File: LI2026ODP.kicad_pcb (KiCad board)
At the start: 4 copper layers, 18.8 x 39.9 mm, 33 parts, among them J1 CON28-B700X1400_DIP, J2 Conn_01x05_Male, U1 MUA08A_TEX, U2 LQFP_0B1KET6_STM, U3 21-0066J_28_MXM

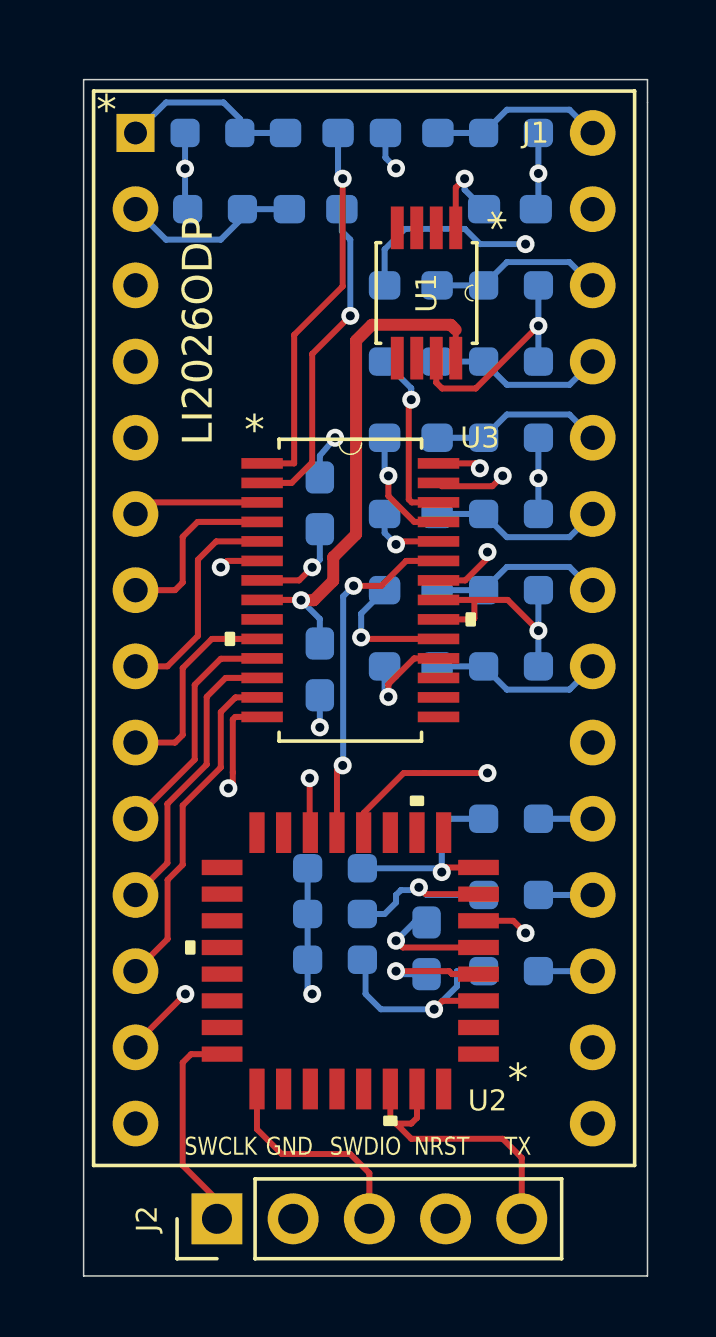
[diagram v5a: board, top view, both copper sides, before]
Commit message: Clean up the wire in the power layer.
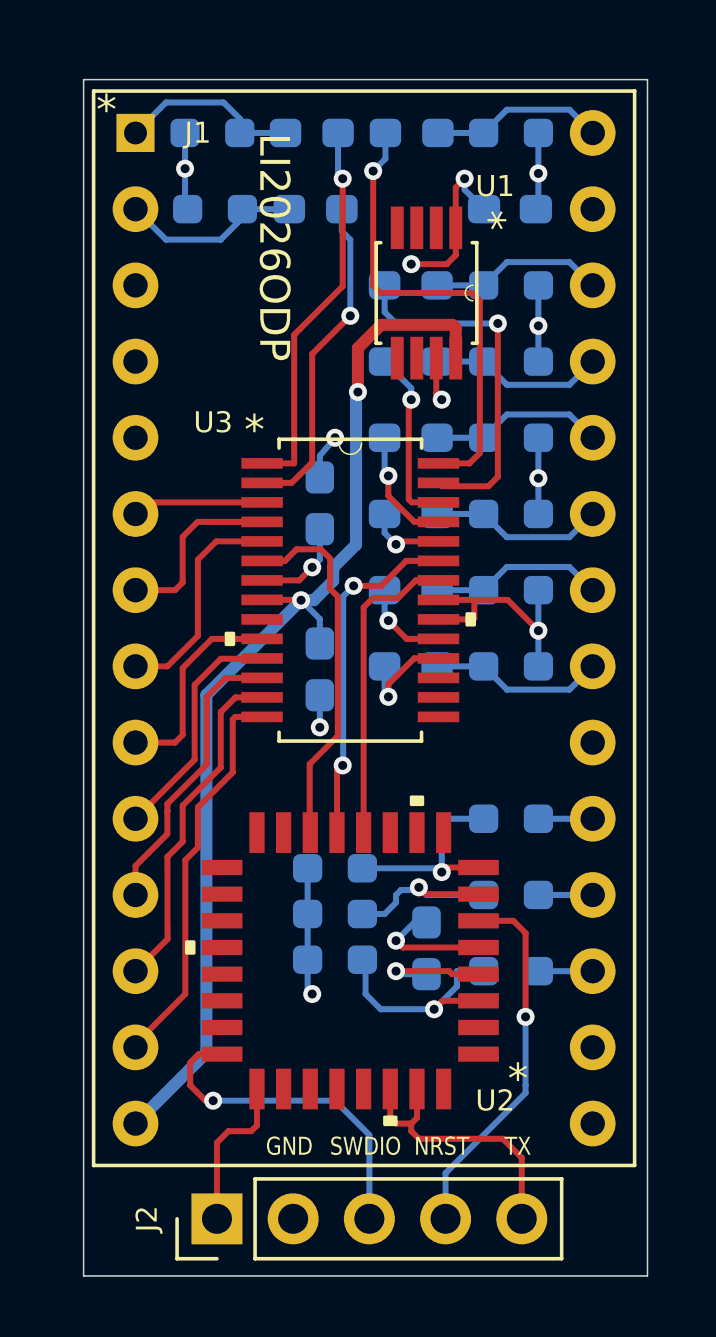
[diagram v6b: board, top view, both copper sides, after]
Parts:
- J1: value CON28-B700X1400_DIP -> 9-1437539-2
- U1: value MUA08A_TEX -> LM2936MM-3.3
- U2: value LQFP_0B1KET6_STM -> STM32G0B1KET6
- U3: value 21-0066J_28_MXM -> max6921aui
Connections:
- U2 pad 24: /SWCLK -> /SWDIO
- U2 pad 25: /SWDIO -> /SWCLK
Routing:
- net /D3: track 16.8 -> 12.1 mm, vias 2 -> 1
- net /SCK: track 14.9 -> 10.5 mm, vias 2 -> 0
- net /SWDIO: track 7.22 -> 11.4 mm, vias 0 -> 1
- net GND: track 34.5 -> 30.8 mm, vias 9 -> 10
- net +3V3: track 10.3 -> 12.8 mm, vias 3 -> 4
- net /D2: track 13.9 -> 15.6 mm, vias 2 -> 1
- net /D7: track 4.50 -> 2.99 mm
- net /SWCLK: track 7.11 -> 5.96 mm
- net /MOSI: track 11.5 -> 12.2 mm, vias 2 -> 0
- net /NRST: track 11.7 -> 12.4 mm
- net /+25V: track 37.0 -> 36.8 mm, vias 1 -> 2
- net /SEG_DP: vias 2 -> 0
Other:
- board text added: "https://github.com/suikan4github/LI2026ODP"
- board text removed: "SWCLK"
